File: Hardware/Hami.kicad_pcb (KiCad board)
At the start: 2 copper layers, 77.5 x 117.5 mm, 48 parts, among them J1 OLED, J2 BAT, SW1 Reset, SW10 MX, SW11 MX, SW12 MX, SW13 MX, SW14 MX, SW15 MX, SW16 MX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

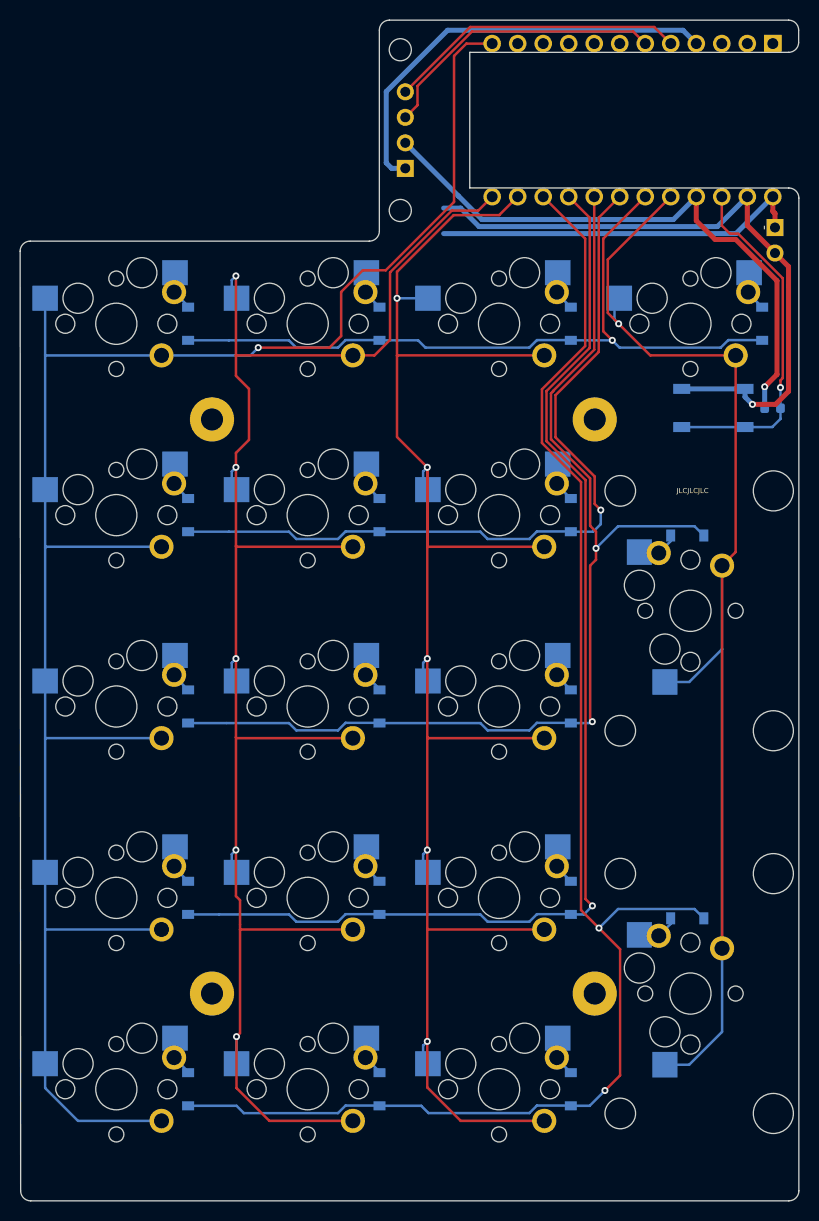
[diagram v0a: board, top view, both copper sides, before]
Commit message: Hami V1.1
Because who doesn't need rotary encoder support in the botton and top left corners? Also re-routed some of the traces.
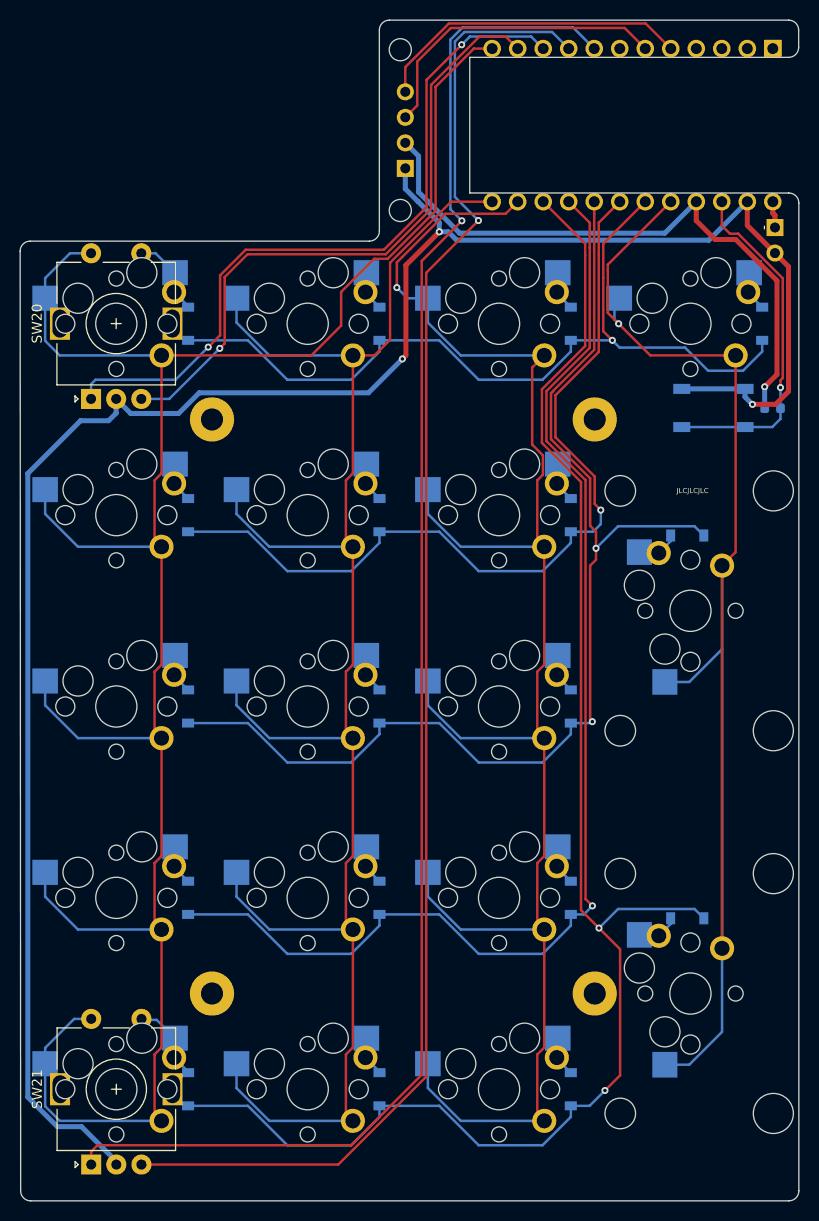
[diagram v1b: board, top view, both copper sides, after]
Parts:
- added SW20: Rot_1, Rotary_Encoder:RotaryEncoder_Alps_EC11E-Switch_Vertical_H20mm, F.Cu at (117.5, 63.5)
- added SW21: Rot_2, Rotary_Encoder:RotaryEncoder_Alps_EC11E-Switch_Vertical_H20mm, F.Cu at (117.5, 139.7)
- moved U1 0.50 mm to (168.9, 43.7)
- renumbered R3 to R1
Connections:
- J1 pad 1: GND2 -> GND
- U1 pad 10: Net-(U1-Pad10) -> Rot_1A
- U1 pad 11: Net-(U1-Pad11) -> Rot_1B
- U1 pad 3: GND2 -> Net-(U1-Pad3)
- U1 pad 4: GND2 -> Net-(U1-Pad4)
- U1 pad 8: Net-(U1-Pad8) -> Rot_2A
- U1 pad 9: Net-(U1-Pad9) -> Rot_2B
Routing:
- net Rot_2A: track 0.00 -> 158.2 mm, vias 0 -> 1
- net Rot_2B: track 0.00 -> 150.6 mm, vias 0 -> 1
- net GND: track 65.6 -> 205.2 mm, vias 1 -> 3
- net Rot_1A: track 0.00 -> 72.2 mm, vias 0 -> 2
- net Rot_1B: track 0.00 -> 64.0 mm, vias 0 -> 1
- net GND2: track 43.2 -> 0.00 mm
- net Net-(J2-Pad1): track 37.5 -> 2.66 mm
- net COL1: track 194.9 -> 227.2 mm, vias 1 -> 0
- net ROW1: track 75.4 -> 84.0 mm
- net ROW3: track 109.8 -> 115.9 mm
- net ROW4: track 117.0 -> 123.1 mm
- net ROW2: track 79.8 -> 85.8 mm
- net ROW5: track 151.3 -> 157.4 mm
- net Net-(D1-Pad2): track 4.05 -> 8.20 mm
- net Net-(D5-Pad2): track 4.05 -> 8.18 mm
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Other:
- outline, holes or cut-outs redrawn
- board text added: "Hami V1.1 Designed by Aria"
- board text removed: "Hami V1.0 Designed by Aria"
